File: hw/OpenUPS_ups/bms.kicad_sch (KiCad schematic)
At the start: 36 parts, among them Q1103 BSS84, Q601 AON7534, U1101 BQ76920PW, U901 π220N31

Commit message: Some work on BMS
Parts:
- added Q1104: BSS84, Package_TO_SOT_SMD:SOT-23, symbol Transistor_FET:BSS84
- added Q601 (x2): 2N7002, Package_TO_SOT_SMD:SOT-23, symbol Transistor_FET:2N7002
- added R608 (x3): 100k, Resistor_SMD:R_0603_1608Metric, symbol Device:R_Small
- added R608: 68k, Resistor_SMD:R_0603_1608Metric, symbol Device:R_Small
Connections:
- net +BATT: now also Q1104.2 (S), R608.1, R608.1
- net -BATT: now also Q601.2 (S)
- net GND: now also Q601.2 (S), R608.2
- net TS: now also R608.2
- net at U1101.20 (ALERT): now also Q601.1 (G)
- new net: Q1104.1 (G), Q601.3 (D), R608.2
- new net: Q1104.3 (D), R608.1
- new net: Q601.3 (D), R608.2
- new net WAKEUP: Q601.1 (G), R608.1
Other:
- note added: "Apply positive pulse to turn on BMS"
- moved on the sheet: C607, C713, D603, Q1103, Q601, R606, R608, R613, U1101

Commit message: BMS work
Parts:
- removed C713: Cf, Capacitor_SMD:C_0603_1608Metric, symbol Device:C_Small
- removed D603: BAT54J, Diode_SMD:D_SOD-323F, symbol Diode:BAT54J
- removed R608: 100k, Resistor_SMD:R_0603_1608Metric, symbol Device:R_Small
- added C?: 10u 16V, Capacitor_SMD:C_1206_3216Metric, symbol Device:C
- added D1002 (x3): BAT54, Package_TO_SOT_SMD:SOT-23, symbol Diode:BAT54W
- added D1108, D1109, D1110, D1111: SMF5V0A, Diode_SMD:D_SMF, symbol Diode:SMF5V0A
- added Q1107: BSS84, Package_TO_SOT_SMD:SOT-23, symbol Transistor_FET:BSS84
- added R608, R713: 10k, Resistor_SMD:R_0603_1608Metric, symbol Device:R_Small
- added R608: 100R, Resistor_SMD:R_0603_1608Metric, symbol Device:R_Small
- added R608: 100k, Resistor_SMD:R_0603_1608Metric, symbol Device:R_Small
- C607: value Cc -> 1u 10V
- C607: value 0R -> 1u 10V
- R606: value Rf -> NM
- R608: value Rc -> 51R
- R608: value NM -> 51R
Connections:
- net +3.3VA: now also D1002.3 (K)
- net +BATT: now also Q1107.2 (S), R608.1, R608.2; no longer R606.2
- net -BATT: now also C?.2
- net GND: now also R608.2
- net at C607.1, R608.1, U1101.17 (VC0): now also D1110.2 (A2)
- net at U1101.10 (BAT): now also C?.1, D1002.3 (K), R608.1; no longer R606.1
- net at C607.1, C607.2, R608.1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: now also D1109.1 (A1), D1111.2 (A2)
- net at C607.1, C607.2, R608.1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: now also D1108.1 (A1), D1109.2 (A2)
- net VC2: now reaches R608.2
- net VC2: now also R606.1
- net at C607.1, R608.1, U1101.12 (VC5): now also D1002.1 (A), D1111.1 (A1)
- net at C607.1, C607.2, R608.1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: now also D1108.2 (A2), D1110.1 (A1)
- net at Q601.3 (D): now also Q1107.1 (G), R608.2
- net at Q601.4 (G), R606.1, R606.2: now also D1002.3 (K)
- net at Q1103.3 (D), R606.2: now also D1002.1 (A)
- net VC3: now reaches R608.2
- net VC3: now also R606.2
- net VC1: now reaches R608.2
- new net: Q1107.3 (D), R713.2
- new net ALERT: D1002.1 (A), R608.1, R713.1
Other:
- note added: "Apply positive pulse to turn on BMS (>2ms) Do not keep it driven high all the time. Boot-up is complete after 10ms max."
- note added: "Connect 10k NTC Return to -BATT Note: It must be present (or at least 10k dummy resistor)"
- note added: "Discrete unidirectional translators"
- note added: "I2C Isolator"
- note added: "Recommended CHG pin protection"
- note added: "Unidirectional translator, only ALERT output is supported."
- note removed: "Apply positive pulse to turn on BMS"
- note removed: "Connect 10k NTC Return to -BATT"
- note removed: "TODO: Hops over GND barrier for ALERT and TS1 pull-up Understanding the CHG switch Ports"
- moved on the sheet: C607, C713, Q1103, Q1104, Q601, R606, R608, R613, U1101

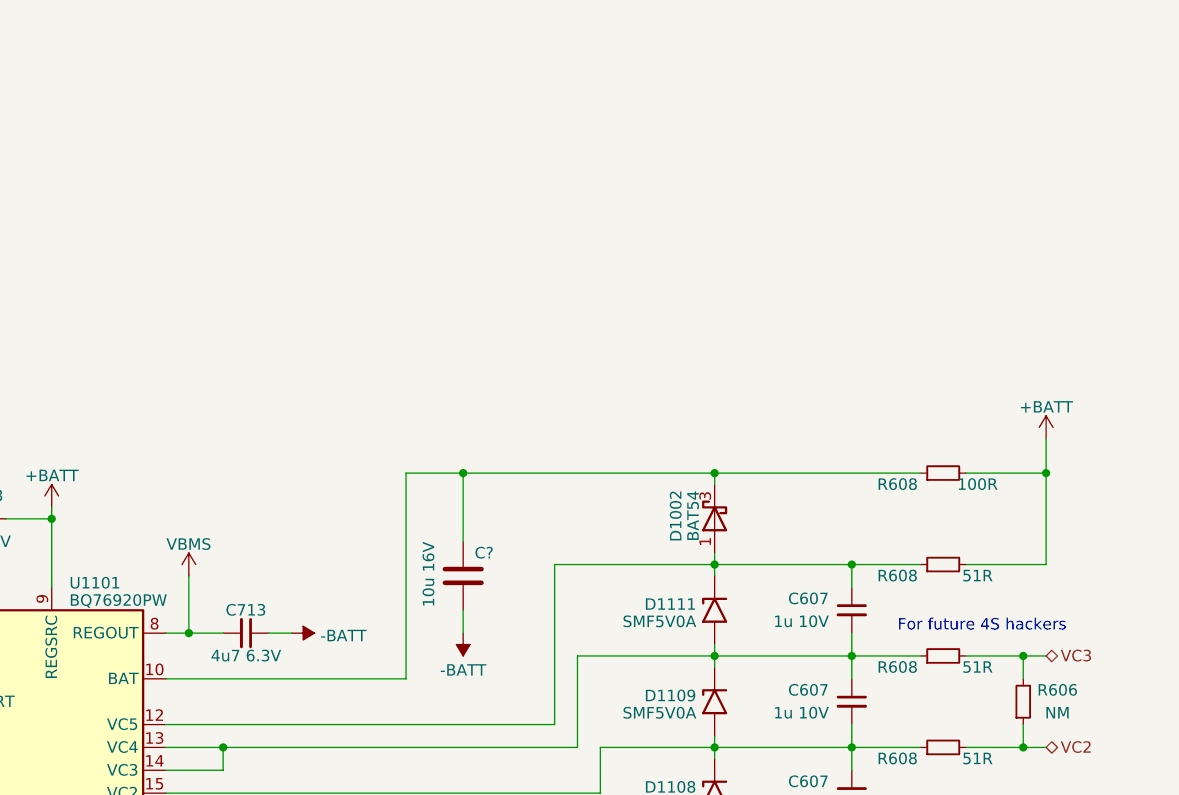
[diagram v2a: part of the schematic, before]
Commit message: BMS implementation complete (on schematic)
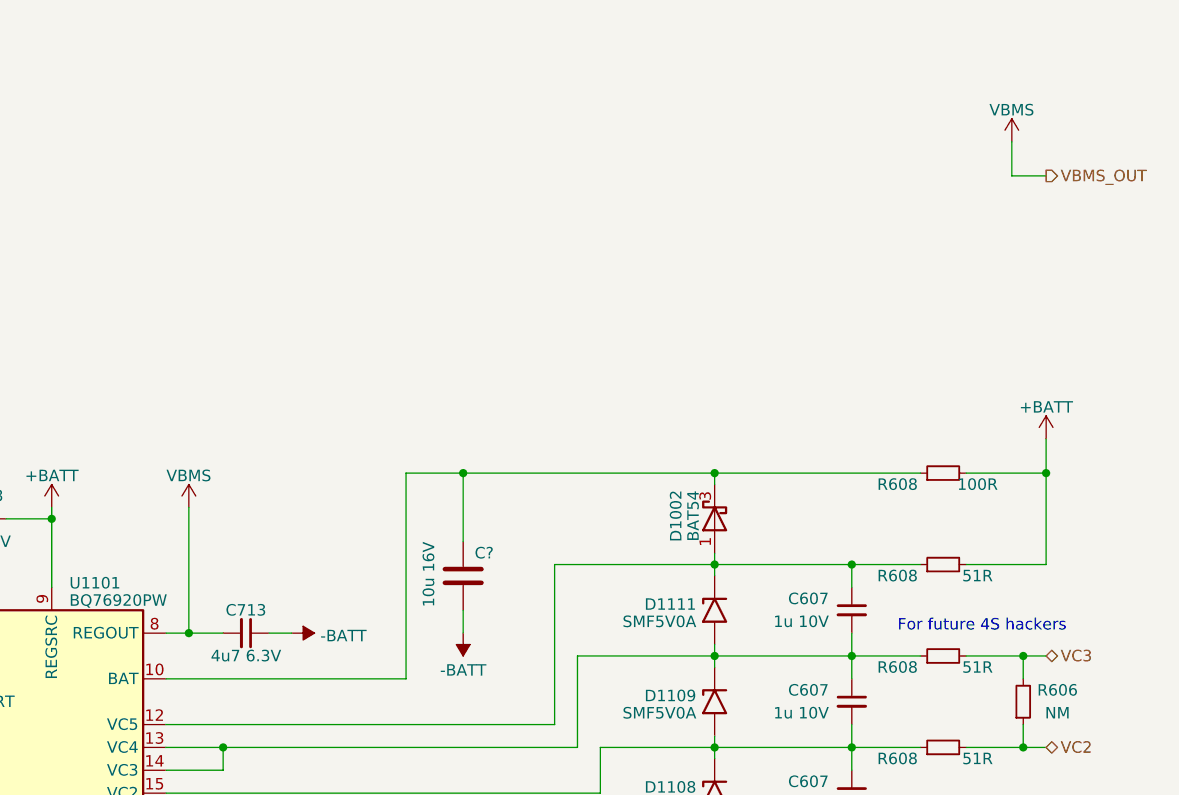
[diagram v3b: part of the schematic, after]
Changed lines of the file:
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@@
+    (stroke (width 0) (type default))
+  )
+  (wire (pts (xy 264.16 35.56) (xy 267.97 35.56))
     (stroke (width 0) (type default))
   )
@@
     (stroke (width 0) (type default))
   )
+  (wire (pts (xy 264.16 31.75) (xy 264.16 35.56))
+    (stroke (width 0) (type default))
+  )
   (wire (pts (xy 246.38 129.54) (xy 254 129.54))
     (stroke (width 0) (type default))
@@
     (stroke (width 0) (type default))
   )
-  (wire (pts (xy 172.72 86.36) (xy 172.72 80.01))
+  (wire (pts (xy 172.72 86.36) (xy 172.72 72.39))
     (stroke (width 0) (type default))
   )
@@
   (hierarchical_label "ALERT" (shape output) (at 45.72 46.99 180) (fields_autoplaced)
     (effects (font (size 1.27 1.27)) (justify right))
+  )
+  (hierarchical_label "VBMS_OUT" (shape output) (at 267.97 35.56 0) (fields_autoplaced)
+    (effects (font (size 1.27 1.27)) (justify left))
   )
   (hierarchical_label "VC3" (shape bidirectional) (at 267.97 88.9 0) (fields_autoplaced)
@@
     )
   )
-  (symbol (lib_id "power:VDD") (at 172.72 80.01 0) (mirror y) (unit 1)
+  (symbol (lib_id "power:VDD") (at 172.72 72.39 0) (mirror y) (unit 1)
     (in_bom yes) (on_board yes) (dnp no) (fields_autoplaced)
-    (property "Reference" "#PWR01110" (at 172.72 83.82 0)
-      (effects (font (size 1.27 1.27)) hide)
-    )
-    (property "Value" "VBMS" (at 172.72 76.5081 0)
-      (effects (font (size 1.27 1.27)))
-    )
-    (property "Footprint" "" (at 172.72 80.01 0)
-      (effects (font (size 1.27 1.27)) hide)
-    )
-    (property "Datasheet" "" (at 172.72 80.01 0)
+    (property "Reference" "#PWR01110" (at 172.72 76.2 0)
+      (effects (font (size 1.27 1.27)) hide)
+    )
+    (property "Value" "VBMS" (at 172.72 68.8881 0)
+      (effects (font (size 1.27 1.27)))
+    )
+    (property "Footprint" "" (at 172.72 72.39 0)
+      (effects (font (size 1.27 1.27)) hide)
+    )
+    (property "Datasheet" "" (at 172.72 72.39 0)
       (effects (font (size 1.27 1.27)) hide)
     )
@@
         )
       )
+    )
+  )
+  (symbol (lib_id "power:VDD") (at 264.16 31.75 0) (mirror y) (unit 1)
+    (in_bom yes) (on_board yes) (dnp no) (fields_autoplaced)
+    (property "Reference" "#PWR01130" (at 264.16 35.56 0)
+      (effects (font (size 1.27 1.27)) hide)
+    )
+    (property "Value" "VBMS" (at 264.16 28.2481 0)
+      (effects (font (size 1.27 1.27)))
+    )
+    (property "Footprint" "" (at 264.16 31.75 0)
+      (effects (font (size 1.27 1.27)) hide)
+    )
+    (property "Datasheet" "" (at 264.16 31.75 0)
+      (effects (font (size 1.27 1.27)) hide)
+    )
+    (pin "1")
+    (instances
+      (project "OpenUPS_ups"
+        (path "/f77faec3-eac4-47f3-a2de-ec4a039f4502/61a2f923-9a9e-4138-95d0-52fecb3d1a29"
+          (reference "#PWR01130") (unit 1)
+        )
+      )

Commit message: PCB multitasking
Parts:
- removed R606: NM, Resistor_SMD:R_0603_1608Metric, symbol Device:R_Small
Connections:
- net BMS_SCL renamed BATT_SCL
- net BMS_SDA renamed BATT_SDA
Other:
- note added: "Apply positive pulse to turn on BMS (>2ms) Do not keep it driven high all the time, this will disrupt temperature measurements. Boot-up is complete after 10ms max."
- note removed: "Apply positive pulse to turn on BMS (>2ms) Do not keep it driven high all the time. Boot-up is complete after 10ms max."
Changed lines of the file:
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@@
   (junction (at 231.14 109.22) (diameter 0) (color 0 0 0 0)
   )
-  (junction (at 265.43 88.9) (diameter 0) (color 0 0 0 0)
-  )
   (junction (at 231.14 88.9) (diameter 0) (color 0 0 0 0)
   )
@@
   (junction (at 111.76 167.64) (diameter 0) (color 0 0 0 0)
   )
-  (junction (at 265.43 99.06) (diameter 0) (color 0 0 0 0)
-  )
   (junction (at 157.48 73.66) (diameter 0) (color 0 0 0 0)
   )
@@
   (junction (at 203.2 68.58) (diameter 0) (color 0 0 0 0)
   )
-  (wire (pts (xy 259.08 99.06) (xy 265.43 99.06))
+  (wire (pts (xy 259.08 99.06) (xy 267.97 99.06))
     (stroke (width 0) (type default))
   )
@@
     (stroke (width 0) (type default))
   )
+  (wire (pts (xy 111.76 175.26) (xy 127 175.26))
+    (stroke (width 0) (type default))
+  )
   (wire (pts (xy 80.01 143.51) (xy 80.01 147.32))
     (stroke (width 0) (type default))
@@
     (stroke (width 0) (type default))
   )
-  (wire (pts (xy 265.43 99.06) (xy 267.97 99.06))
-    (stroke (width 0) (type default))
-  )
   (wire (pts (xy 93.98 167.64) (xy 85.09 167.64))
     (stroke (width 0) (type default))
   )
+  (wire (pts (xy 102.87 180.34) (xy 127 180.34))
+    (stroke (width 0) (type default))
+  )
   (wire (pts (xy 111.76 168.91) (xy 111.76 167.64))
     (stroke (width 0) (type default))
@@
     (stroke (width 0) (type default))
   )
-  (wire (pts (xy 259.08 88.9) (xy 265.43 88.9))
+  (wire (pts (xy 259.08 88.9) (xy 267.97 88.9))
     (stroke (width 0) (type default))
   )
@@
     (stroke (width 0) (type default))
   )
-  (wire (pts (xy 265.43 96.52) (xy 265.43 99.06))
-    (stroke (width 0) (type default))
-  )
   (wire (pts (xy 110.49 68.58) (xy 110.49 69.85))
     (stroke (width 0) (type default))
@@
     (stroke (width 0) (type default))
   )
-  (wire (pts (xy 265.43 88.9) (xy 267.97 88.9))
-    (stroke (width 0) (type default))
-  )
   (wire (pts (xy 22.86 182.88) (xy 22.86 186.69))
     (stroke (width 0) (type default))
@@
     (stroke (width 0) (type default))
   )
-  (wire (pts (xy 116.84 180.34) (xy 102.87 180.34))
-    (stroke (width 0) (type default))
-  )
   (wire (pts (xy 215.9 88.9) (xy 231.14 88.9))
     (stroke (width 0) (type default))
@@
     (stroke (width 0) (type default))
   )
-  (wire (pts (xy 116.84 175.26) (xy 111.76 175.26))
-    (stroke (width 0) (type default))
-  )
   (wire (pts (xy 231.14 68.58) (xy 254 68.58))
     (stroke (width 0) (type default))
@@
   )
   (wire (pts (xy 36.83 167.64) (xy 45.72 167.64))
-    (stroke (width 0) (type default))
-  )
-  (wire (pts (xy 265.43 88.9) (xy 265.43 91.44))
     (stroke (width 0) (type default))
   )
@@
     (fill (type none))
   )
-  (rectangle (start 15.24 156.21) (end 128.27 195.58)
+  (rectangle (start 15.24 156.21) (end 139.7 195.58)
     (stroke (width 0) (type dash))
     (fill (type none))
@@
     (effects (font (size 1.27 1.27)) (justify left bottom))
   )
-  (text "Apply positive pulse to turn on BMS (>2ms)\nDo not keep it driven high all the time.\nBoot-up is complete after 10ms max."
-    (at 17.78 95.25 0)
+  (text "Apply positive pulse to turn on BMS (>2ms)\nDo not keep it driven high all the time,\nthis will disrupt temperature measurements.\nBoot-up is complete after 10ms max."
+    (at 17.78 96.52 0)
     (effects (font (size 1.27 1.27)) (justify left bottom))
   )
@@
     (effects (font (size 1.27 1.27)) (justify left bottom))
   )
-  (label "BMS_SDA" (at 116.84 175.26 0) (fields_autoplaced)
+  (label "BMS_SDA" (at 114.3 175.26 0) (fields_autoplaced)
     (effects (font (size 1.27 1.27)) (justify left bottom))
   )
-  (label "BMS_SCL" (at 116.84 180.34 0) (fields_autoplaced)
+  (label "BMS_SCL" (at 114.3 180.34 0) (fields_autoplaced)
     (effects (font (size 1.27 1.27)) (justify left bottom))
   )
@@
     (effects (font (size 1.27 1.27)) (justify right))
   )
+  (hierarchical_label "BATT_SCL" (shape bidirectional) (at 127 180.34 0) (fields_autoplaced)
+    (effects (font (size 1.27 1.27)) (justify left))
+  )
   (hierarchical_label "VC1" (shape bidirectional) (at 267.97 109.22 0) (fields_autoplaced)
     (effects (font (size 1.27 1.27)) (justify left))
@@
   )
   (hierarchical_label "VBMS_OUT" (shape output) (at 267.97 35.56 0) (fields_autoplaced)
+    (effects (font (size 1.27 1.27)) (justify left))
+  )
+  (hierarchical_label "BATT_SDA" (shape bidirectional) (at 127 175.26 0) (fields_autoplaced)
     (effects (font (size 1.27 1.27)) (justify left))
   )
@@
         )
       )
-    )
-  )
-  (symbol (lib_id "Device:R_Small") (at 265.43 93.98 0) (mirror x) (unit 1)
-    (in_bom yes) (on_board yes) (dnp no)
-    (property "Reference" "R606" (at 269.24 92.71 0)
-      (effects (font (size 1.27 1.27)))
-    )
-    (property "Value" "NM" (at 269.24 95.25 0)
-      (effects (font (size 1.27 1.27)))
-    )
-    (property "Footprint" "Resistor_SMD:R_0603_1608Metric" (at 265.43 93.98 0)
-      (effects (font (size 1.27 1.27)) hide)
-    )
-    (property "Datasheet" "~" (at 265.43 93.98 0)
-      (effects (font (size 1.27 1.27)) hide)
-    )
-    (pin "1")
-    (pin "2")
-    (instances
-      (project "OpenUPS_ups"
-        (path "/f77faec3-eac4-47f3-a2de-ec4a039f4502/09fcd86a-cc7e-4bce-97cb-42a94055ba63"
-          (reference "R606") (unit 1)
-        )
-        (path "/f77faec3-eac4-47f3-a2de-ec4a039f4502/dfbaaed0-e564-4e21-900d-d5a65c0f1694"
-          (reference "R306") (unit 1)
-        )
-        (path "/f77faec3-eac4-47f3-a2de-ec4a039f4502/61a2f923-9a9e-4138-95d0-52fecb3d1a29"
-          (reference "R1128") (unit 1)
-        )
-      )
